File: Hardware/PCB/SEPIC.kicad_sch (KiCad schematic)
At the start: 25 parts, among them Q1 IRF7807, U1 LM3478MA

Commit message: Update SEPIC PCB design and layout
This change refreshes the KiCad SEPIC board data after reworking the PCB layout and component placement. It updates the schematic and PCB files to reflect the new footprints, test points, diode and passive components, and adjusts the project metadata and layer visibility settings used by KiCad.
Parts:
- removed D2: MBRS130LT3, Diode_SMD:D_1206_3216Metric, symbol Device:D_Schottky
- added D4: SS32, Diode_SMD:D_SMA, symbol Diode:SS32
- added TP3: GND_out, TestPoint:TestPoint_THTPad_4.0x4.0mm_Drill2.0mm, symbol Connector:TestPoint
- added TP4: GND_in, TestPoint:TestPoint_THTPad_4.0x4.0mm_Drill2.0mm, symbol Connector:TestPoint
- C2: footprint (none) -> Capacitor_SMD:CP_Elec_8x10
- C3, C4: value 15u -> 22u; footprint (none) -> Capacitor_SMD:CP_Elec_6.3x5.8
- D1: footprint Resistor_SMD:R_1206_3216Metric -> LED_SMD:LED_1206_3216Metric
- L1, L2: footprint (none) -> Inductor_SMD:L_Vishay_IHLP-2020
- Q1: footprint (none) -> Package_SO:SOIC-8_5.3x5.3mm_P1.27mm
- RV1: footprint (none) -> Potentiometer_THT:Potentiometer_Bourns_3296W_Vertical
- TP1, TP2: footprint Connector_Pin:Pin_D1.0mm_L10.0mm -> TestPoint:TestPoint_Plated_Hole_D2.0mm
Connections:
- net GND: now also TP3.1, TP4.1
- net Vout: now also D4.1 (K)
- net at C5.1, L1.2: now also D4.2 (A)

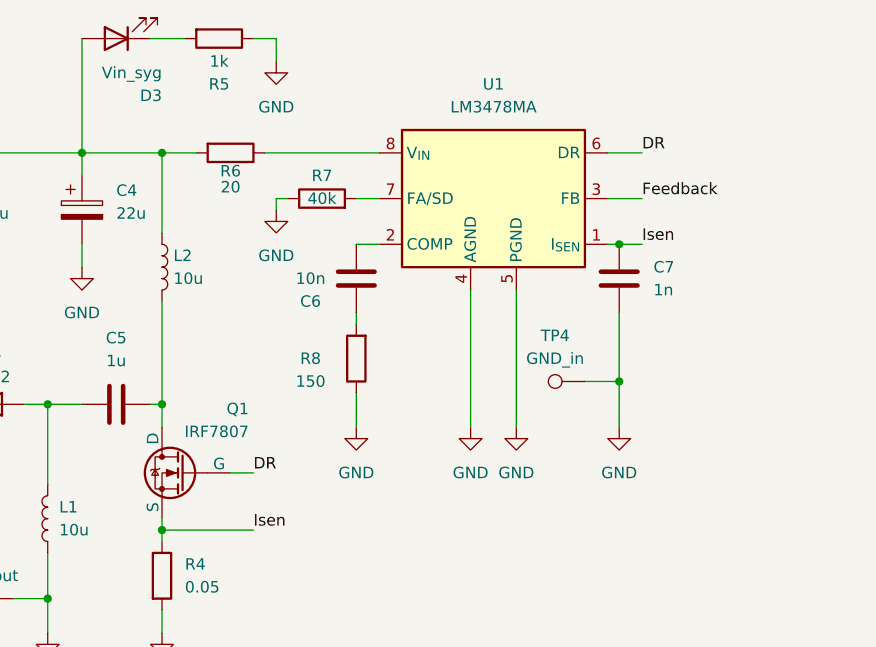
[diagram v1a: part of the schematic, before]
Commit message: Add C8; update footprints, routing, schematic
Added capacitor C8 (1206) to PCB and schematic and created Hardware/PCB/SEPIC.png. Updated many footprint positions, silk labels and power symbols (#PWR17), adjusted routing (new segments, vias, some trace widths increased), and refined filled copper polygons. Schematic updated with new wires/junctions and an embedded board image. Also changed project prefs (active_layer) and recorded used_designators in .kicad_pro.
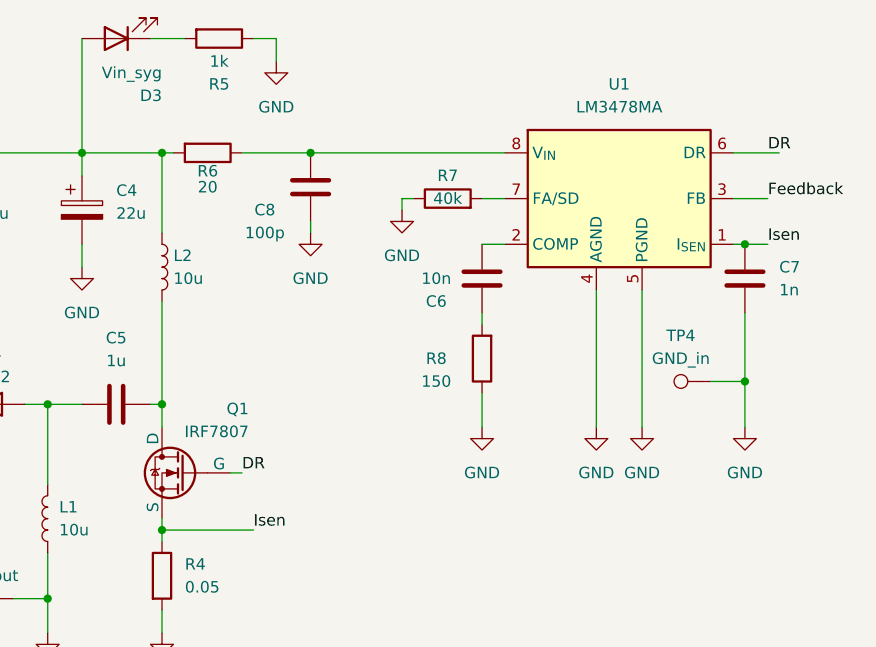
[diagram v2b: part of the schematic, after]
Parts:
- added C8: 100p, Capacitor_SMD:C_1206_3216Metric, symbol Device:C
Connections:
- net GND: now also C8.2
- net at R6.1, U1.8 (V_{IN}): now also C8.1
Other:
- moved on the sheet: C6, C7, R6, R7, R8, TP4, U1

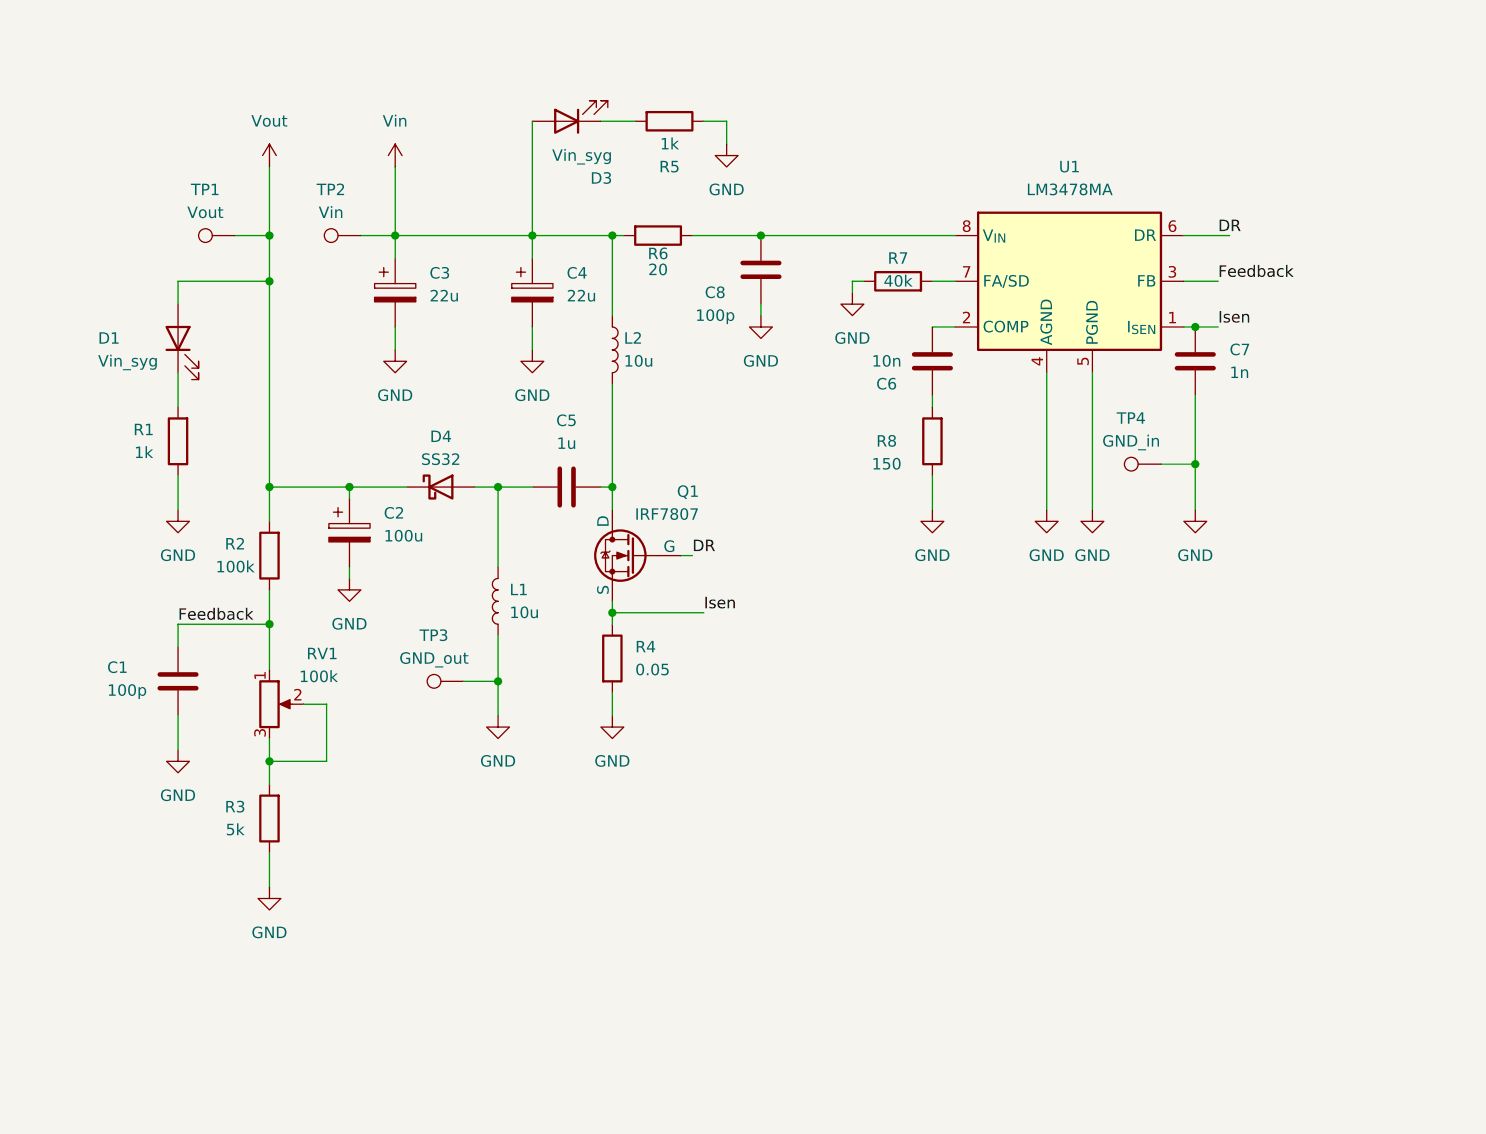
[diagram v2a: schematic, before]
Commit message: Added reverse voltage protection
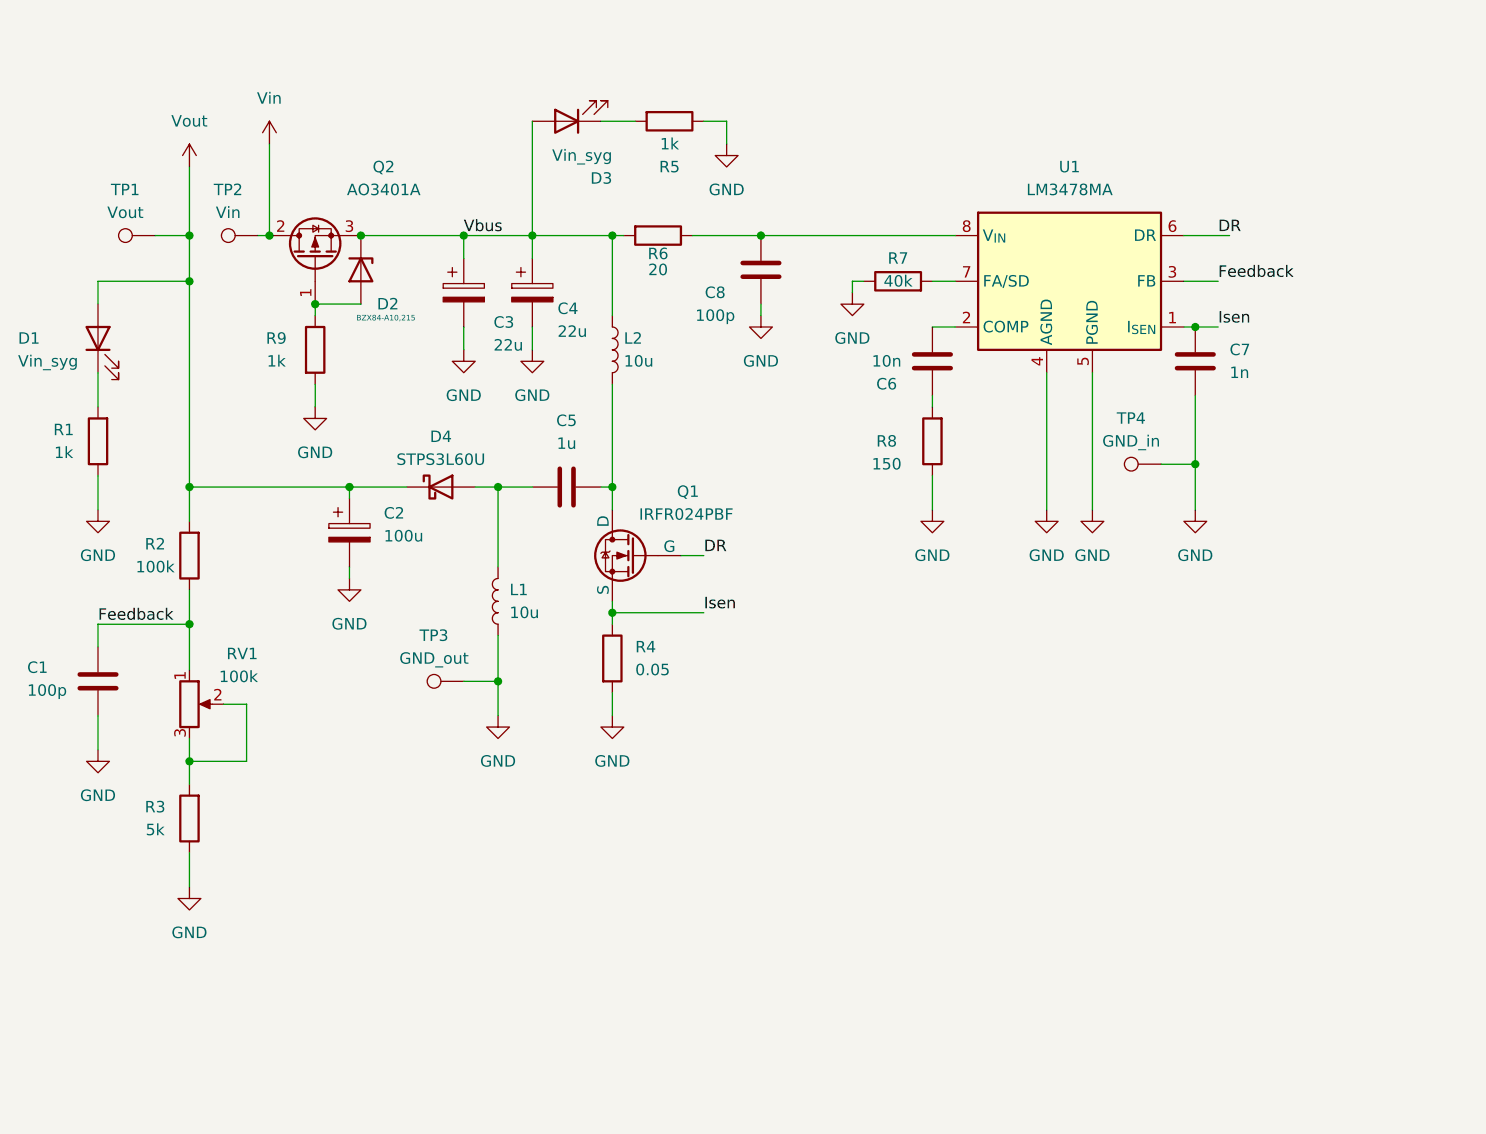
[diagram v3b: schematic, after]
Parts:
- added D2: BZX84-A10,215, Package_TO_SOT_SMD:SOT-23, symbol Device:D_Zener
- added Q2: AO3401A, Package_TO_SOT_SMD:SOT-23, symbol Transistor_FET:Q_PMOS_GDS
- added R9: 1k, Resistor_SMD:R_1206_3216Metric, symbol Device:R
- D4: value SS32 -> STPS3L60U; footprint Diode_SMD:D_SMA -> Diode_SMD:D_SMB
- Q1: value IRF7807 -> IRFR024PBF; footprint Package_SO:SOIC-8_5.3x5.3mm_P1.27mm -> IRFR024:IRFR024PBF
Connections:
- net GND: now also R9.2
- net Vin: now also Q2.2 (D); no longer C3.1, C4.1, D3.2 (A), L2.1, R6.2
- new net: D2.2 (A), Q2.1 (G), R9.1
- new net Vbus: C3.1, C4.1, D2.1 (K), D3.2 (A), L2.1, Q2.3 (S), R6.2
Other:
- moved on the sheet: C1, C3, D1, R1, R2, R3, RV1, TP1, TP2

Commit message: Fixed reverse voltage protection footprints
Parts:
- D2: footprint Package_TO_SOT_SMD:SOT-23 -> BZX84:SOT-23
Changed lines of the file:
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@@
 			)
 		)
-		(property "Footprint" "Package_TO_SOT_SMD:SOT-23"
+		(property "Footprint" "BZX84:SOT-23"
 			(at 60.96 41.91 0)
 			(hide yes)

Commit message: Update PCB footprints, layout and schematic positions
Replace/standardize several footprints (LM3478 -> SOIC-8, DPAK MOSFET removed, Vishay IHLP inductor footprint added), adjust silkscreen references and pad positions, retune pad nets, add vias, routing segments and copper zones, and tidy fp_line/fp_poly outlines. Synchronize schematic symbol coordinates to match new PCB placement. Also update SEPIC.kicad_pro used_designators (added D5,Z1). These edits reorganize the SEPIC board layout and BOM footprints for manufacturability and correct net/pin assignments.
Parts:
- C6: value 10n -> 100n
- C8: value 100p -> 100n
- R2: value 100k -> 15k
- R3: value 5k -> 1k
- R4: value 0.05 -> 1m
- R7: value 40k -> 120k
- R8: value 150 -> 1
- RV1: value 100k -> 10k
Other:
- moved on the sheet: C1, C2, C3, C4, C5, C6, C7, C8, D1, D2, D3, D4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

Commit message: update and backup
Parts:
- R1: value 1k -> 2.2k
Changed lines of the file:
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@@
 			)
 		)
-		(property "Value" "1k"
+		(property "Value" "2.2k"
 			(at 44.45 59.69 0)
 			(show_name no)

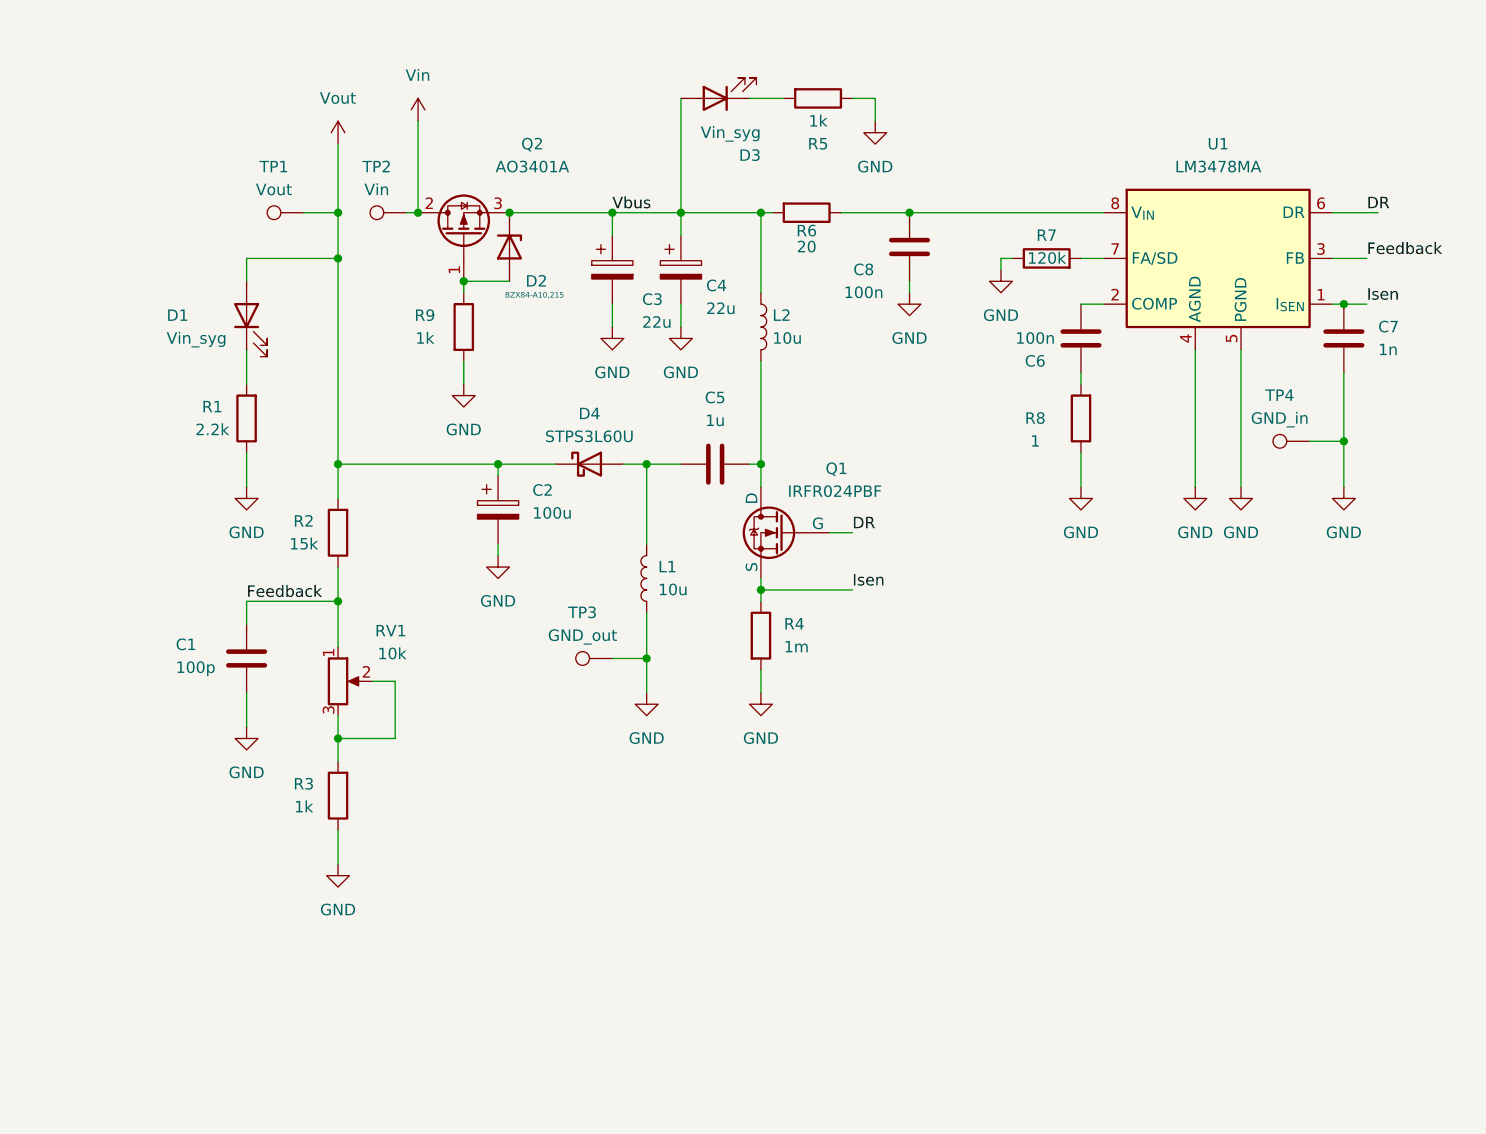
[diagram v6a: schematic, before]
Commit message: Calculation value update
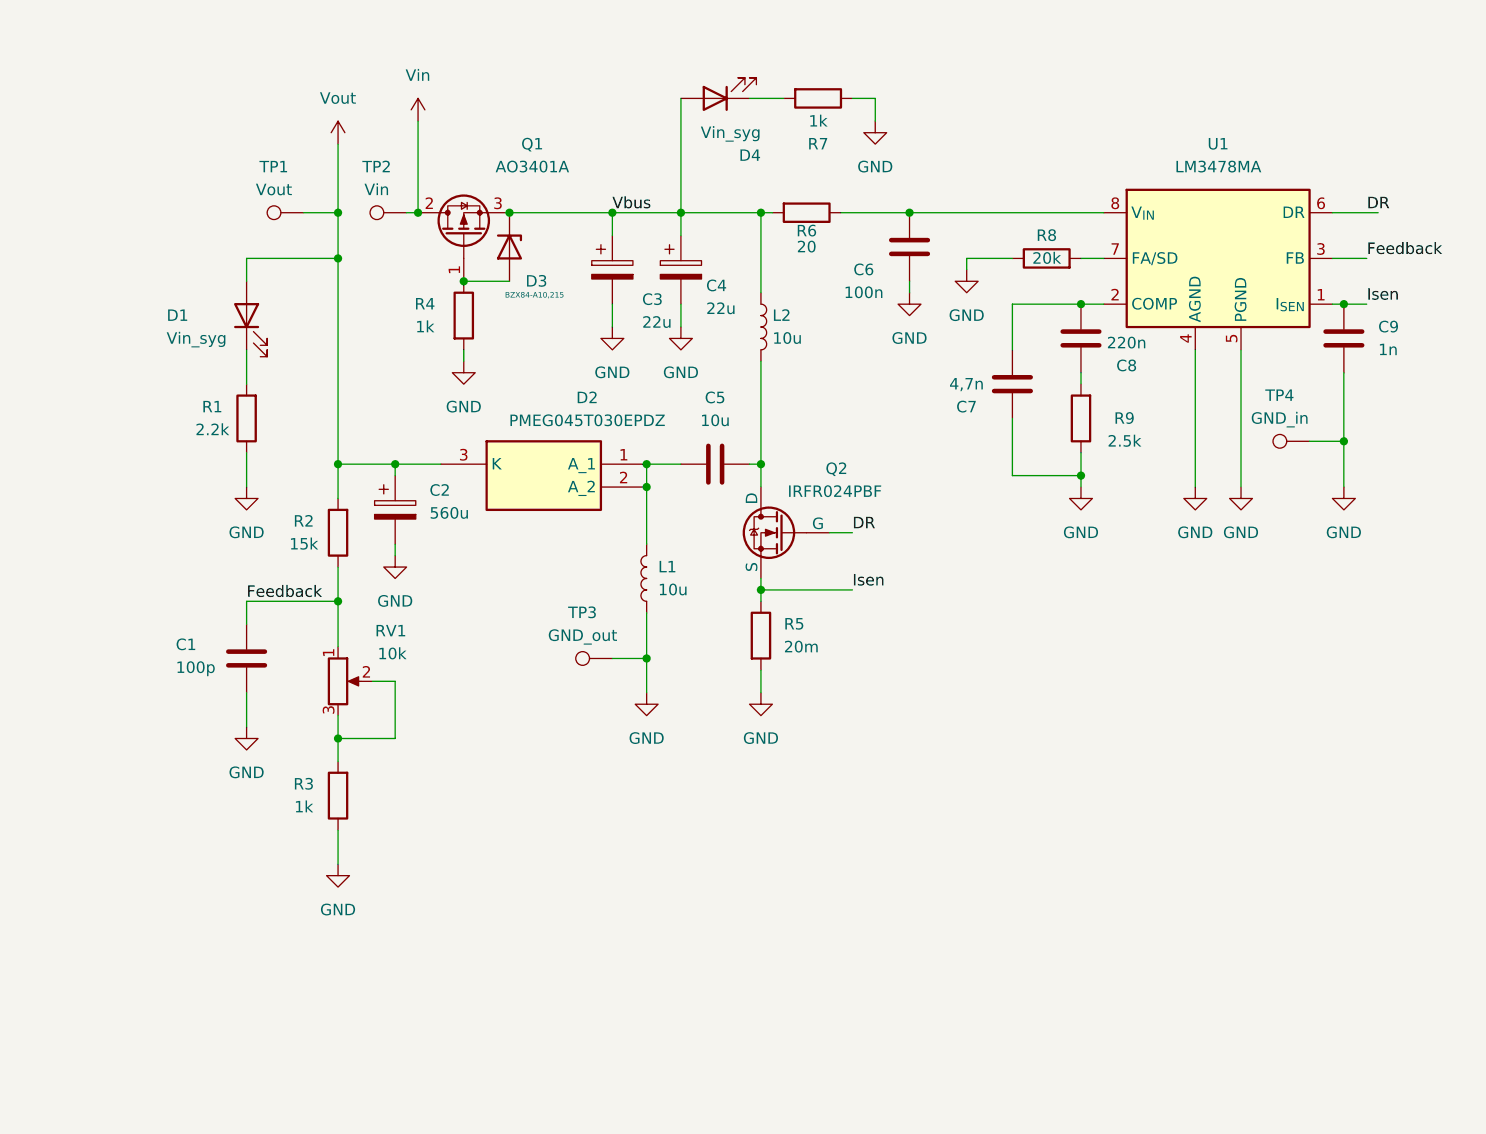
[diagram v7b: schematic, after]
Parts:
- removed D4: STPS3L60U, Diode_SMD:D_SMB, symbol Diode:SS32
- added C7: 4,7n, Capacitor_SMD:C_1206_3216Metric, symbol Device:C
- added D2: PMEG045T030EPDZ, Package_TO_SOT_SMD:Nexperia_CFP15_SOT-1289, symbol PMEG045T030EPDZ:PMEG045T030EPDZ
- C2: value 100u -> 560u
- C5: value 1u -> 10u
- C8: renamed from C6; value 100n -> 220n
- R5: renamed from R4; value 1m -> 20m
- R8: renamed from R7; value 120k -> 20k
- R9: renamed from R8; value 1 -> 2.5k
- renumbered C8 to C6, C7 to C9, D2 to D3, D3 to D4, Q2 to Q1, Q1 to Q2, R9 to R4, R5 to R7
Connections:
- net GND: now also C7.1
- net Vout: now also D2.3 (K)
- net at C8.2, U1.2 (COMP): now also C7.2
- net at C5.1, L1.2: now also D2.1 (A_1), D2.2 (A_2)
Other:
- moved on the sheet: C2, R4
